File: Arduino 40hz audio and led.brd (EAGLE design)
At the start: 79.2 x 109.7 mm, 38 parts, among them IC1 LM7805, IC2 IRL-Z44N, IC3 LM741

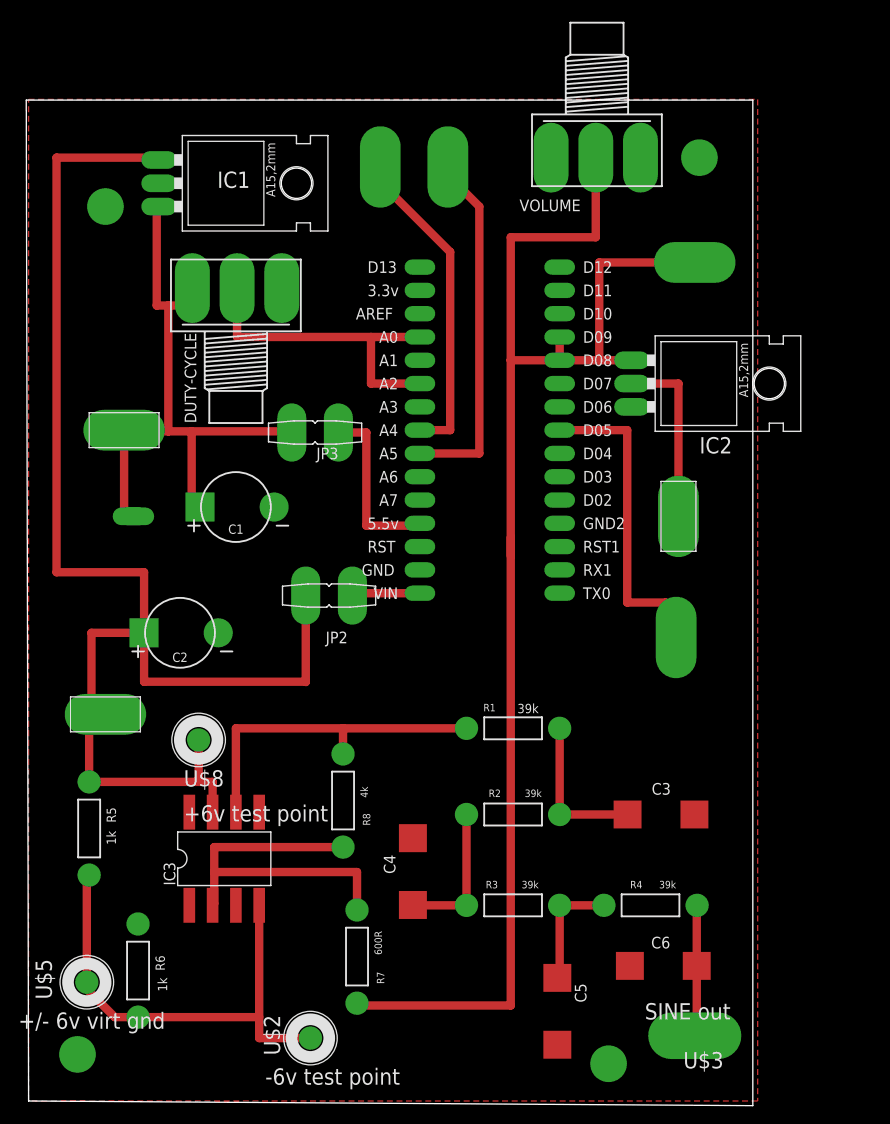
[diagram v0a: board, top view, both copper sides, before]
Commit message: Should be final surface mount commit
This should be the final surface mount commit before making a new
version of the board with 'proper' through hole parts.
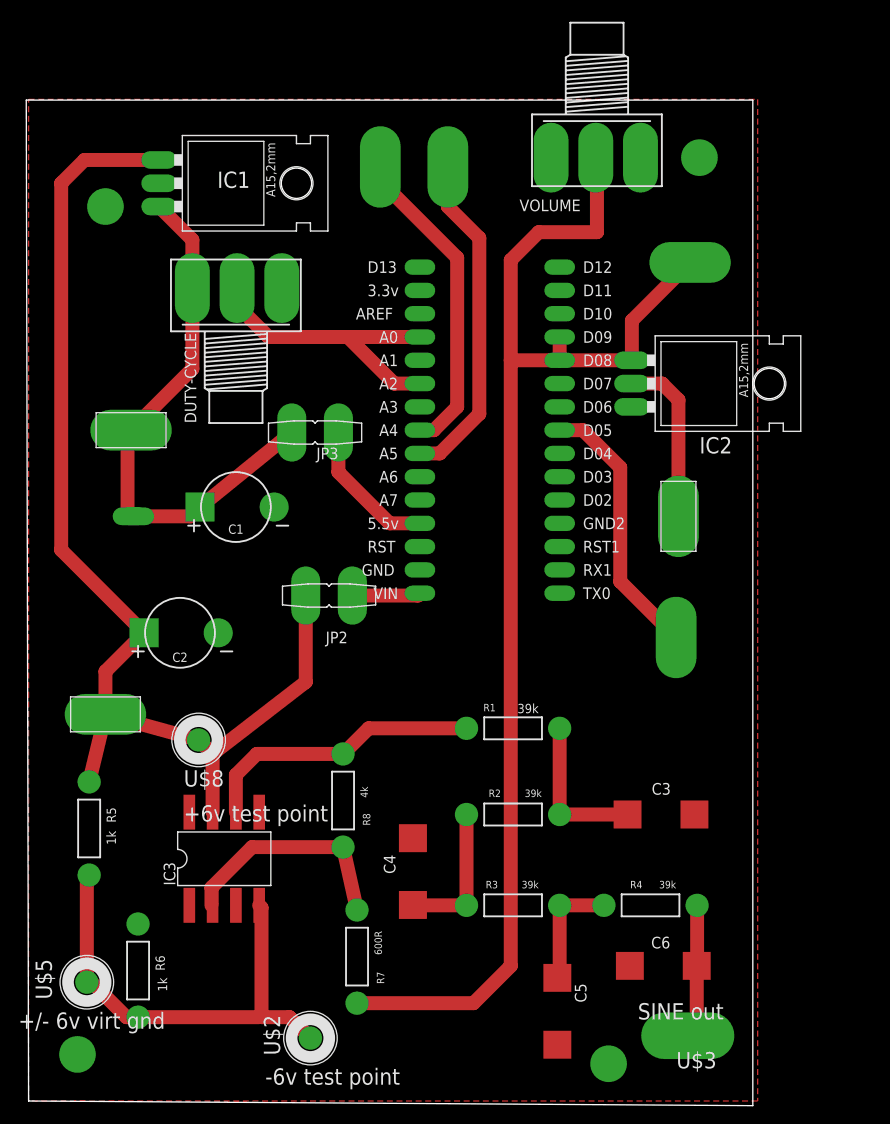
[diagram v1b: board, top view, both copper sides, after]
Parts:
- moved P+2 0.76 mm to (10.9, 73.4)
- moved U$3 0.76 mm to (71.6, 7.37)
- moved U$14 0.51 mm to (71.9, 91.7)
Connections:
- net N$14: now also U$4.PAD$1
- net N$15: now also U$6.PAD$1
- net N$6: now also U$3.PAD$1
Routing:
- net +12V: track 150.0 -> 124.0 mm
- net N$10: track 40.4 -> 25.4 mm
- net N$2: track 159.0 -> 145.2 mm
- net +5V: track 85.7 -> 78.1 mm
- net N$13: track 37.1 -> 31.3 mm
- net N$9: track 19.3 -> 15.5 mm
- net N$11: track 32.3 -> 29.4 mm
- net N$1: track 33.8 -> 31.3 mm
- net N$12: track 52.7 -> 50.2 mm
- net N$8: track 9.43 -> 7.47 mm
- net N$15: track 38.3 -> 36.6 mm

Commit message: First commit after creating thruhole branch
This is the first commit after changing parts and the board for a
thru-hole design.
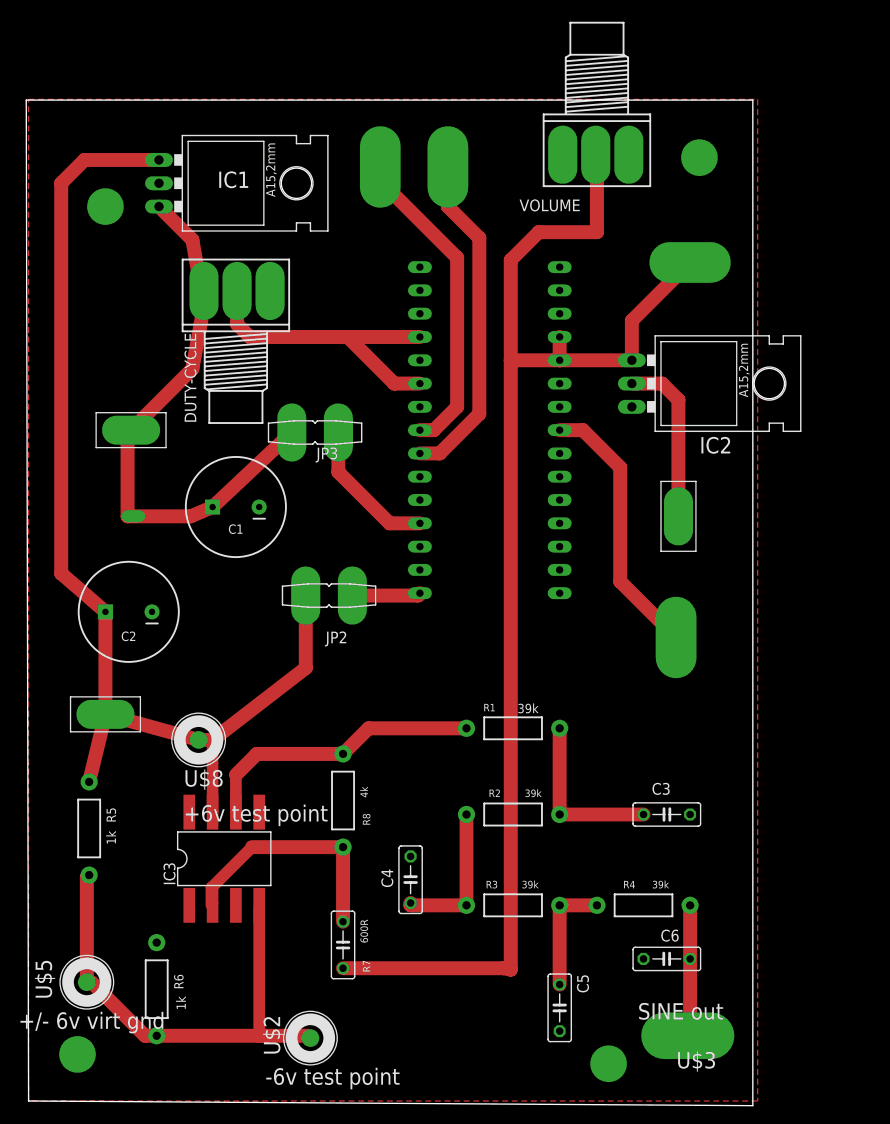
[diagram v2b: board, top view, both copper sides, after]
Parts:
- C1, C2: device jim_muppet_parts:CAP-POLARIZED -> SparkFun-Passives:CPOL-RADIAL-1000UF-25V
- C3, C4, C5, C6: device jim_muppet_parts:CAP-MEDIUM-MUPPET -> rcl:C050-025X075
- IC1, IC2: device jim_muppet_parts:78XXL -> SparkFun-PowerIC:78XXL
- R1, R2, R3, R4, R5, R6, R8: device jim_muppet_parts:AXIAL-0.4 -> SparkFun-Passives:AXIAL-0.4
- R7: device jim_muppet_parts:AXIAL-0.4 -> rcl:C050-025X075
- moved C2 6.04 mm to (10.7, 53.6)
- moved R6 2.87 mm to (13.7, 12.4)
- moved R7 1.98 mm to (34.0, 17.3)
- moved C4 1.55 mm to (41.4, 24.4)
- moved C6 1.27 mm to (69.3, 15.7)
- moved C5 1.05 mm to (57.7, 10.4)
- moved R4 0.76 mm to (66.8, 21.6)
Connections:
- net N$10: now also R7.1; no longer R7.P$1
- net N$2: now also R7.2; no longer R7.P$2
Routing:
- net +12V: track 124.0 -> 120.1 mm
- net N$12: track 50.2 -> 52.9 mm
- net N$3: track 16.8 -> 18.5 mm
- net N$1: track 31.3 -> 32.5 mm
- net N$10: track 25.4 -> 26.5 mm

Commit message: See Diff for changes
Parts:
- moved C2 34.1 mm to (8.89, 87.6)
- moved P+2 1.61 mm to (12.4, 73.9), turned to 90 degrees
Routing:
- net +5V: track 78.4 -> 77.9 mm
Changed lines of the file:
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@@
 <param name="mtCopper" value="0.035mm 0.035mm 0.035mm 0.035mm 0.035mm 0.035mm 0.035mm 0.035mm 0.035mm 0.035mm 0.035mm 0.035mm 0.035mm 0.035mm 0.035mm 0.035mm"/>
 <param name="mtIsolate" value="1.5mm 0.15mm 0.2mm 0.15mm 0.2mm 0.15mm 0.2mm 0.15mm 0.2mm 0.15mm 0.2mm 0.15mm 0.2mm 0.15mm 0.2mm"/>
-<param name="mdWireWire" value="0.6mm"/>
-<param name="mdWirePad" value="0.6mm"/>
+<param name="mdWireWire" value="0.7mm"/>
+<param name="mdWirePad" value="0.7mm"/>
 <param name="mdWireVia" value="0.6mm"/>
 <param name="mdPadPad" value="0.6mm"/>
@@
 <attribute name="NAME" x="22.352" y="63.119" size="1.016" layer="25" font="vector" ratio="20" rot="R180" align="bottom-center"/>
 </element>
-<element name="C2" library="SparkFun-Passives" package="CPOL-RADIAL-1000UF-25V" value="100uF" x="10.668" y="53.594" smashed="yes" rot="R180">
-<attribute name="NAME" x="10.668" y="51.435" size="1.016" layer="25" font="vector" ratio="20" rot="R180" align="bottom-center"/>
+<element name="C2" library="SparkFun-Passives" package="CPOL-RADIAL-1000UF-25V" value="100uF" x="8.89" y="87.63" smashed="yes" rot="R180">
+<attribute name="NAME" x="8.89" y="85.471" size="1.016" layer="25" font="vector" ratio="20" rot="R180" align="bottom-center"/>
 </element>
 <element name="C3" library="rcl" library_urn="urn:adsk.eagle:library:334" package="C050-025X075" package3d_urn="urn:adsk.eagle:package:23637/1" value="100nF" x="69.342" y="31.496" smashed="yes">
@@
 </element>
 <element name="U$1" library="jim_muppet_parts" package="ARDUINO-NANO" value="ARDUINO-NANO" x="52.578" y="64.516" smashed="yes"/>
-<element name="P+2" library="jim_muppet_parts" package="POWER-IN-PAD" value="+5V" x="10.922" y="73.406" smashed="yes"/>
+<element name="P+2" library="jim_muppet_parts" package="POWER-IN-PAD" value="+5V" x="12.446" y="73.914" smashed="yes" rot="R90"/>
 <element name="DUTY-CYCLE" library="jim_muppet_parts" package="POTENTIOMETER" package3d_urn="urn:adsk.eagle:package:22726/1" value="10K" x="22.352" y="87.884" smashed="yes">
 <attribute name="NAME" x="18.034" y="74.168" size="1.27" layer="25" rot="R90"/>
@@
 <contactref element="U$8" pad="P$1"/>
 <wire x1="29.972" y1="47.469778125" x2="29.943778125" y2="47.498" width="0.9144" layer="1"/>
-<wire x1="3.302" y1="100.33" x2="3.302" y2="57.781878125" width="1.524" layer="1"/>
+<wire x1="3.302" y1="100.33" x2="3.302" y2="90.274975" width="1.524" layer="1"/>
 <wire x1="29.972" y1="55.372" x2="29.972" y2="47.469778125" width="1.524" layer="1"/>
 <wire x1="19.812" y1="31.75" x2="19.812" y2="39.624" width="1.27" layer="1"/>
@@
 <wire x1="6.35" y1="35.052" x2="8.128" y2="42.418" width="1.524" layer="1"/>
 <wire x1="19.812" y1="39.624" x2="29.972" y2="47.469778125" width="1.524" layer="1"/>
-<wire x1="8.128" y1="42.418" x2="8.128" y2="53.594" width="1.524" layer="1"/>
-<wire x1="8.128" y1="53.594" x2="3.302" y2="57.781878125" width="1.524" layer="1"/>
+<wire x1="6.35" y1="87.63" x2="6.35" y2="44.196" width="1.524" layer="1"/>
+<wire x1="8.128" y1="42.418" x2="6.35" y2="44.196" width="1.524" layer="1"/>
+<wire x1="6.35" y1="87.63" x2="3.302" y2="90.274975" width="1.524" layer="1"/>
 <wire x1="13.97" y1="102.87" x2="5.842" y2="102.87" width="1.524" layer="1"/>
 <wire x1="5.842" y1="102.87" x2="3.302" y2="100.33" width="1.524" layer="1"/>
@@
 <contactref element="DUTY-CYCLE" pad="1"/>
 <contactref element="JP3" pad="2"/>
-<wire x1="10.922" y1="73.406" x2="10.922" y2="73.279" width="0.9144" layer="1"/>
 <contactref element="IC2" pad="GND"/>
 <contactref element="P+3" pad="VCC"/>
@@
 <wire x1="17.419" y1="64.008" x2="10.541" y2="64.008" width="1.524" layer="1"/>
 <contactref element="U$7" pad="PAD$1"/>
-<wire x1="10.541" y1="64.008" x2="10.541" y2="73.025" width="1.524" layer="1"/>
-<wire x1="10.541" y1="73.025" x2="10.922" y2="73.406" width="1.524" layer="1"/>
+<wire x1="10.541" y1="64.008" x2="10.541" y2="71.53275" width="1.524" layer="1"/>
+<wire x1="12.446" y1="73.914" x2="10.541" y2="71.53275" width="1.524" layer="1"/>
 <wire x1="18.876" y1="86.995" x2="17.606" y2="94.154" width="1.524" layer="1"/>
 <wire x1="17.606" y1="94.154" x2="13.97" y2="97.79" width="1.524" layer="1"/>
-<wire x1="10.922" y1="73.406" x2="17.606" y2="80.09" width="1.524" layer="1"/>
-<wire x1="17.606" y1="80.09" x2="18.876" y2="86.995" width="1.524" layer="1"/>
+<wire x1="12.446" y1="73.914" x2="17.621465625" y2="80.17409375" width="1.524" layer="1"/>
+<wire x1="17.621465625" y1="80.17409375" x2="18.876" y2="86.995" width="1.524" layer="1"/>
 <wire x1="28.448" y1="73.152" x2="65.532" y2="78.486" width="0" layer="19" extent="1-1"/>
 </signal>

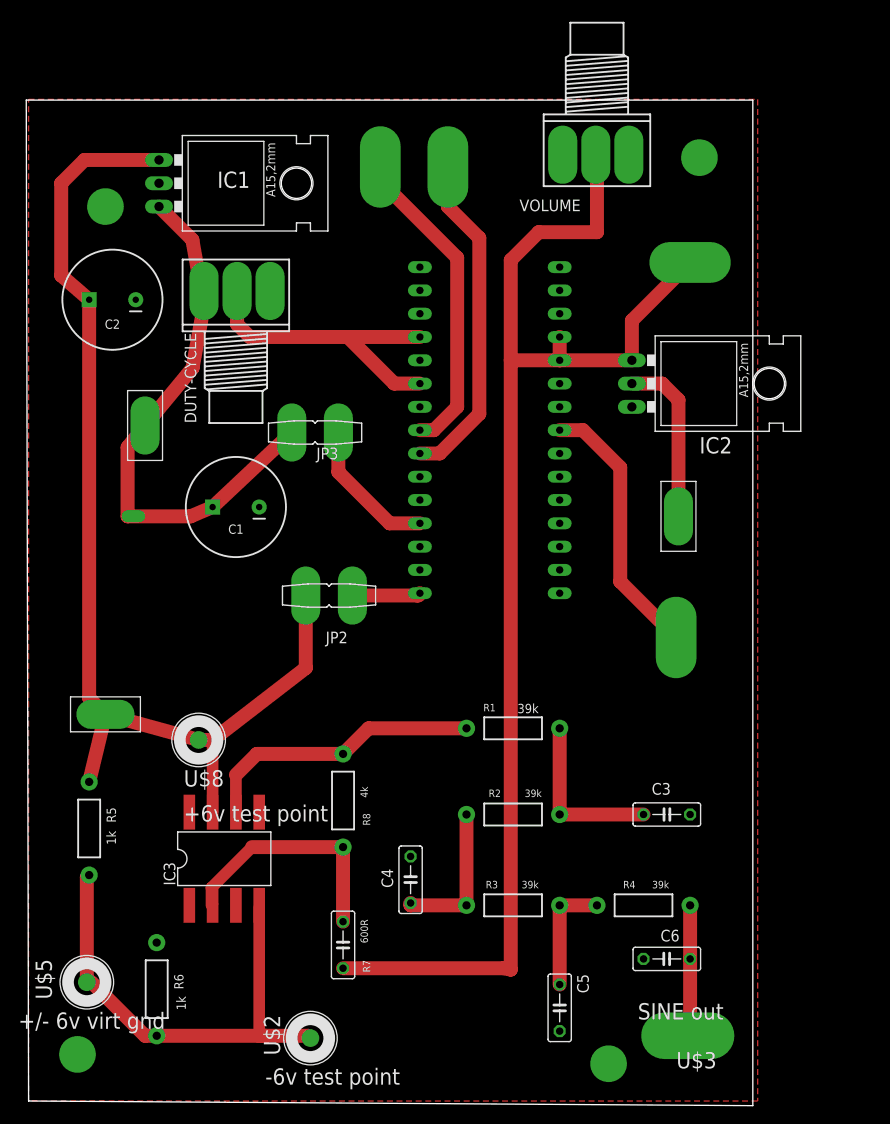
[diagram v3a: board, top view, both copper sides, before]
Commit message: First version of moving traces to the bottom.
First version of moving traces to the bottom.

Now to figure out how to mill this correctly, I'm guessing I need to
mirror it when I do the tools.  Anyway future Jim will judge how this
went.
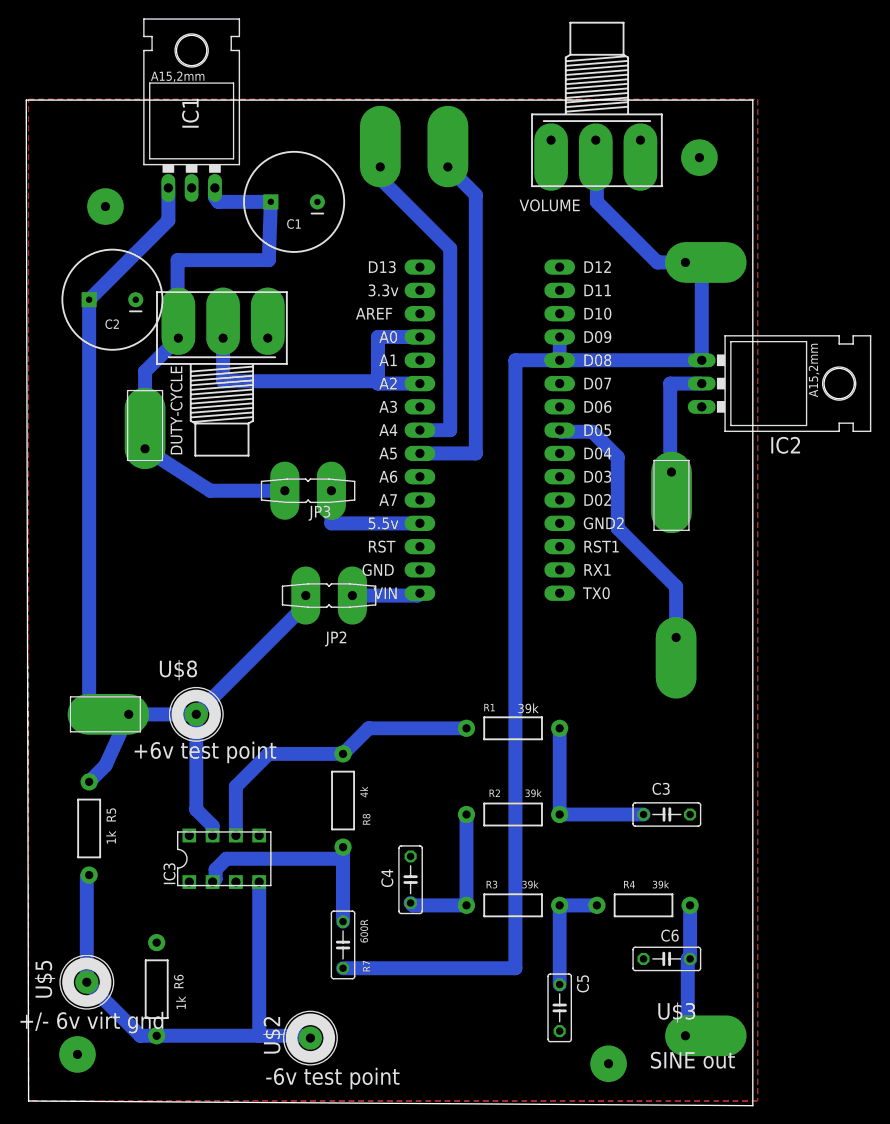
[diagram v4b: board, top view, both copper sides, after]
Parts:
- removed U$7: PAD-2PIN-RECTANGLE, jim_muppet_parts:PAD-2PIN-RECTANGLE-50MIL
- DUTY-CYCLE, VOLUME: device jim_muppet_parts:POTENTIOMETER -> jim_muppet_parts:POTENTIOMETER-THRUHOLE
- IC3: device jim_muppet_parts:DIL08 -> jim_muppet_parts:DIL08-THRUHOLE
- JP2, JP3: device jim_muppet_parts:JP1 -> jim_muppet_parts:JP1-THRUHOLE
- P+1: value +12V -> (none); device jim_muppet_parts:POWER-IN-PAD -> jim_muppet_parts:POWER-IN-PAD-THRUHOLE
- P+2: value +5V -> (none); device jim_muppet_parts:POWER-IN-PAD -> jim_muppet_parts:POWER-IN-PAD-THRUHOLE
- P+3: value +6V -> (none); device jim_muppet_parts:POWER-IN-PAD -> jim_muppet_parts:POWER-IN-PAD-THRUHOLE
- U$1: value ARDUINO-NANO -> (none); device jim_muppet_parts:ARDUINO-NANO -> jim_muppet_parts:ARDUINO-NANO-THRUHOLE
- U$10, U$11, U$12, U$13: value DRILL-HOLE-4MM -> DRILL-HOLE-4MMTHRUHOLE; device jim_muppet_parts:DRILL-HOLE-4MM -> jim_muppet_parts:DRILL-HOLE-4MM-THRUHOLE
- U$14, U$4, U$6, U$9: device jim_muppet_parts:PAD-RECTANGLE-175MIL -> jim_muppet_parts:PAD-RECTANGLE-175MIL-THRUHOLE
- U$2, U$5, U$8: device jim_muppet_parts:PROBE_POINT_1 -> jim_muppet_parts:PROBE_POINT_1-THRUHOLE
- U$3: device jim_muppet_parts:PAD-RECTANGLE-200MIL -> jim_muppet_parts:PAD-RECTANGLE-175MIL-THRUHOLE
- moved C1 33.9 mm to (28.7, 98.3)
- moved IC2 7.62 mm to (77.0, 78.5)
- moved JP3 6.40 mm to (30.2, 66.8)
- moved DUTY-CYCLE 3.87 mm to (20.8, 84.3)
- moved IC1 3.31 mm to (17.5, 103.6), turned to 0 degrees
- moved U$8 2.81 mm to (21.8, 39.9)
- moved P+3 2.41 mm to (69.8, 66.3), turned to 270 degrees
- moved U$14 0.51 mm to (71.4, 91.7)
- moved U$3 0.25 mm to (71.4, 7.37), turned to 0 degrees
- turned U$9 to 270 degrees
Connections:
- net +12V: now also IC3.P$7; no longer IC3.7
- net +5V: no longer U$7.PAD$1
- net N$10: now also IC3.P$2; no longer IC3.2
- net N$12: now also IC3.P$4; no longer IC3.4
- net N$13: now also IC3.P$6; no longer IC3.6
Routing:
- net N$2: track 145.5 -> 137.8 mm
- net +12V: track 120.1 -> 113.2 mm
- net +5V: track 77.9 -> 81.2 mm
- net N$1: track 32.5 -> 35.6 mm
- net N$12: track 52.9 -> 55.5 mm
- net N$10: track 26.5 -> 24.0 mm
- net N$9: track 15.5 -> 13.2 mm
- net N$15: track 36.6 -> 38.6 mm
- net N$13: track 31.3 -> 33.1 mm
- net N$14: track 34.8 -> 33.9 mm
